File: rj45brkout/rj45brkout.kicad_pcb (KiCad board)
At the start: 4 copper layers, 27.7 x 20.3 mm, 19 parts, among them J101 RJ45_LEDS, P101 CONN_01X01, P102 CONN_01X01, P103 CONN_01X01, P104 CONN_01X01, P105 CONN_01X01, P106 CONN_01X01, P107 CONN_01X01, P108 CONN_01X01, P109 CONN_01X01, P110 CONN_01X01, P111 CONN_01X01, P112 CONN_01X01

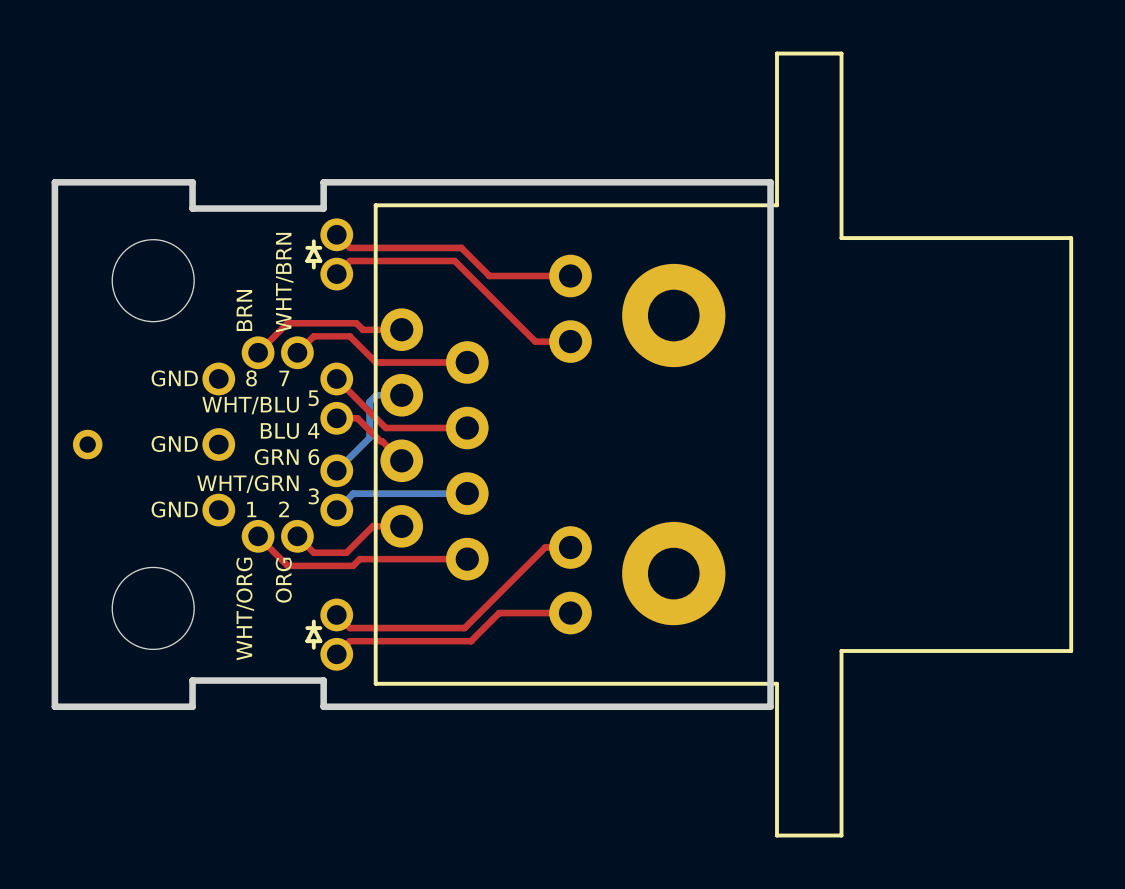
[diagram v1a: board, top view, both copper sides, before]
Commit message: Update rj45brkout design to KiCad 8.
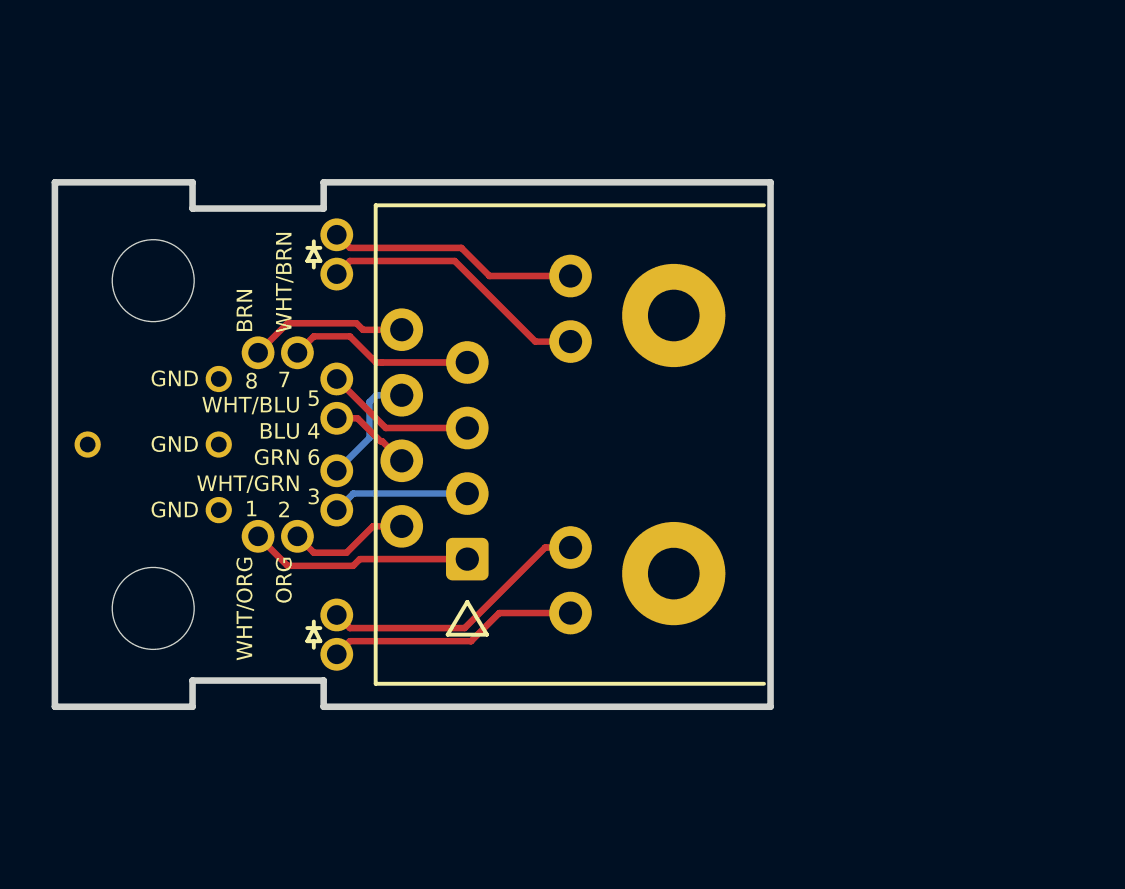
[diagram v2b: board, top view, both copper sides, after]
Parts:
- J101: footprint local:rj45-8-pm -> Local:rj45-8-pm
- P101, P102, P103, P104, P105, P106, P107, P108, P109, P110, P111, P112: footprint local:wire_50x30mil -> Local:wire_50x30mil
- REF** (x2): footprint local:MountingHole_125mil -> Local:MountingHole_125mil
- REF** (x4): footprint local:Stitching_Via_40x24mil -> Local:Stitching_Via_40x24mil
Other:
- net class Default removed
- net class minimum removed
- board text added: "dsun7c4osh@gmail.com"
- board text removed: "dcsun88osh@gmail.com"

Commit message: Bump version string of rj45brkout to v1.1.0.
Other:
- board text added: "v1.1.0"
- board text removed: "v1.0.0"
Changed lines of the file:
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@@
 	(title_block
 		(title "RJ45 panel mount breakout")
-		(date "2018-04-19")
-		(rev "v1.0.0")
+		(date "2025-01-27")
+		(rev "v1.1.0")
 	)
 	(layers
@@
 		)
 	)
-	(gr_text "v1.0.0"
+	(gr_text "v1.1.0"
 		(at 152.146 101.6 0)
 		(layer "B.SilkS")
